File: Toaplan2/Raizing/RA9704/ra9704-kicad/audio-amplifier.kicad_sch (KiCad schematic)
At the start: 42 parts, among them U818 NJM2060, U821 YM3014B, U822 YM3012, U825 NJM2060, U826 TA8201AK

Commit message: fix(ra9704): Add Os as a proxy for 0s in all reference designators
RA9704 has reference designators such that each number has a preceding zero (e.g. RA076, U074, etc.). This causes a bug in KiCAD.

This is 'fixed' by using the 'O' (the letter 'Oh') character instead.

For more info, see the following issue on the KiCAD Gitlab repo

https://gitlab.com/kicad/code/kicad/-/issues/19229
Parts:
- renumbered C81 to CO81, C810 to CO810, C811 to CO811, C812 to CO812, C815 to CO815, C816 to CO816, C817 to CO817, C818 to CO818, C819 to CO819, C82 to CO82, C820 to CO820, C83 to CO83, C84 to CO84, C85 to CO85, C86 to CO86, C87 to CO87, C88 to CO88, C89 to CO89, R81 to RO81, R810 to RO810, R811 to RO811, R812 to RO812, R813 to RO813, R814 to RO814, R815 to RO815, R816 to RO816, R817 to RO817, R818 to RO818, R82 to RO82, R83 to RO83, R84 to RO84, R85 to RO85, R86 to RO86, R87 to RO87, R88 to RO88, R89 to RO89, U818 to UO818, U821 to UO821, U822 to UO822, U825 to UO825, U826 to UO826, VR81 to VRO81

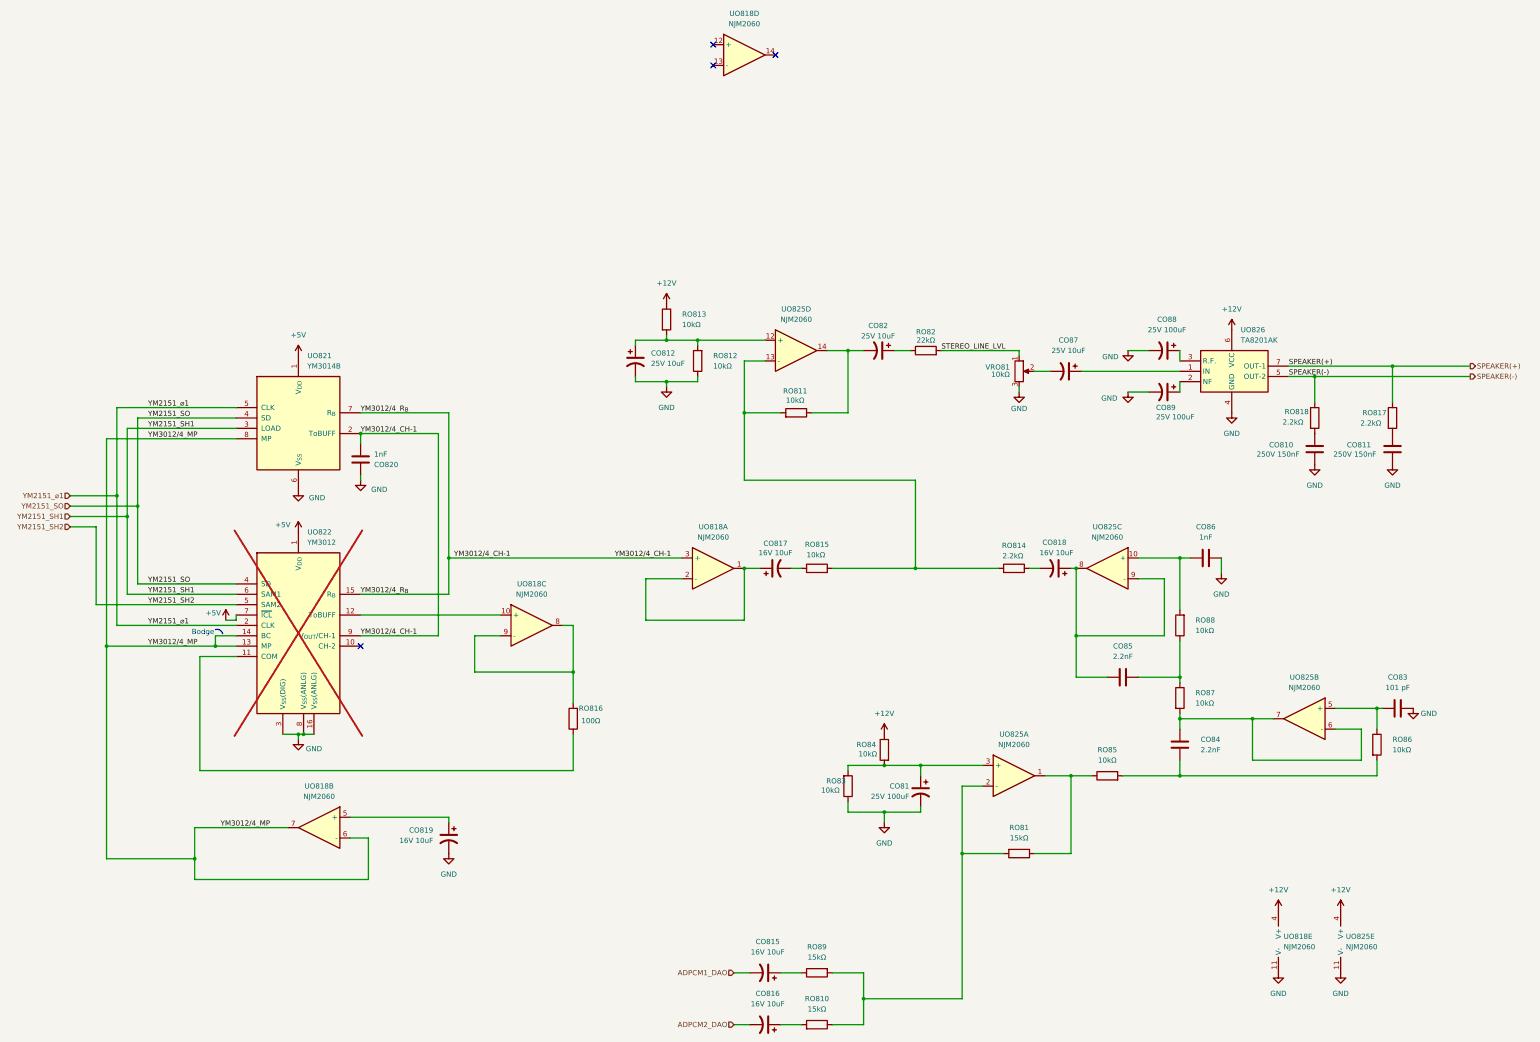
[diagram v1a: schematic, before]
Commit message: doc(ra9704): group 66 ceramic power caps and label on JAMMA page; replace uF with mu symbol
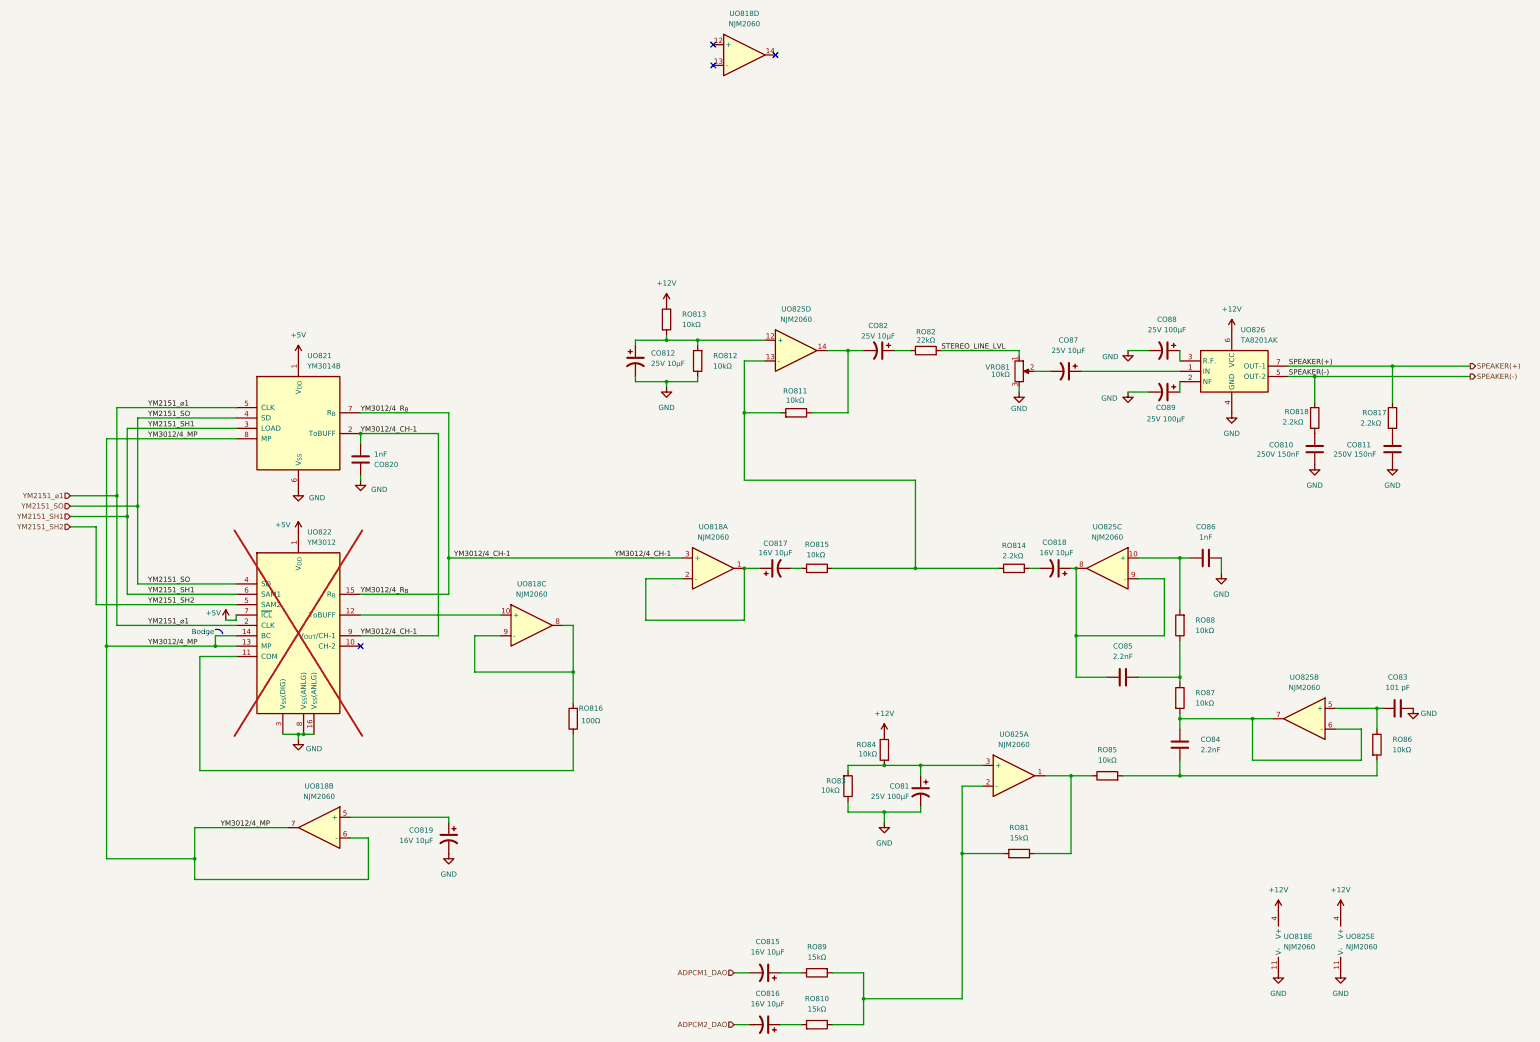
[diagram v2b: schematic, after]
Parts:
- CO81, CO88, CO89: value 25V 100uF -> 25V 100μF
- CO812, CO82, CO87: value 25V 10uF -> 25V 10μF
- CO815, CO816, CO817, CO818, CO819: value 16V 10uF -> 16V 10μF
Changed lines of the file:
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@@
 			)
 		)
-		(property "Value" "16V 10uF"
+		(property "Value" "16V 10μF"
 			(at 217.805 214.63 90)
 			(effects
@@
 			)
 		)
-		(property "Value" "16V 10uF"
+		(property "Value" "16V 10μF"
 			(at 217.805 201.93 90)
 			(effects
@@
 			)
 		)
-		(property "Value" "25V 100uF"
-			(at 312.928 70.866 90)
+		(property "Value" "25V 100μF"
+			(at 310.642 71.374 90)
 			(effects
 				(font
@@
 			)
 		)
-		(property "Value" "16V 10uF"
+		(property "Value" "16V 10μF"
 			(at 219.71 104.14 90)
 			(effects
@@
 			)
 		)
-		(property "Value" "16V 10uF"
+		(property "Value" "16V 10μF"
 			(at 288.544 104.14 90)
 			(effects
@@
 			)
 		)
-		(property "Value" "25V 10uF"
+		(property "Value" "25V 10μF"
 			(at 291.465 54.61 90)
 			(effects
@@
 			)
 		)
-		(property "Value" "25V 100uF"
+		(property "Value" "25V 100μF"
 			(at 315.595 49.53 90)
 			(effects
@@
 			)
 		)
-		(property "Value" "25V 100uF"
+		(property "Value" "25V 100μF"
 			(at 252.476 163.83 0)
 			(effects
@@
 			)
 		)
-		(property "Value" "25V 10uF"
+		(property "Value" "25V 10μF"
 			(at 189.23 57.7849 0)
 			(effects
@@
 			)
 		)
-		(property "Value" "25V 10uF"
+		(property "Value" "25V 10μF"
 			(at 244.856 51.054 90)
 			(effects
@@
 			)
 		)
-		(property "Value" "16V 10uF"
+		(property "Value" "16V 10μF"
 			(at 135.89 174.6249 0)
 			(effects
